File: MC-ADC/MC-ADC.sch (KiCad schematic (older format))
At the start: 11 parts, among them J1 86094327313755E1LF, U2 SZCM1213A-04SO

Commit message: ADC
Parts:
- removed C?: C_Small, symbol Device:C_Small
- removed R?: R_Small_US, symbol Device:R_Small_US
- removed U?: LM324DTBR2G, symbol MC-ADC:LM324DTBR2G
- added C?: C_Small, symbol Device:C_Small
- added R?: R_Small_US, symbol Device:R_Small_US
- added U?: LM339DR, symbol MC-ADC:LM339DR
- U?: symbol MC-ADC:LM324DTBR2G -> MC-ADC-rescue:LM324DTBR2G-MC-ADC
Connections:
- net labels added: -12V, ADCIN1, ADCIN2, ADCIN3, SAFE_STATE_FLAG
- net labels removed: ADCINA2, ADCINA4, ADCINB2
- wire segments 161 -> 232
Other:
- note added: "Edge Connector - Amphenol\nNeed to update\n"
- note added: "notes\n"
- note removed: "Edge Connector - Amphenol"
- moved on the sheet: C1, J1, R1, R2, R3, R4

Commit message: ADC Work
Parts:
- removed U2: SZCM1213A-04SO, symbol MC-ADC:SZCM1213A-04SO
- removed U?: LM339DR, symbol MC-ADC:LM339DR
- added R? (x6): 1.5K, symbol Device:R_Small_US
- added R? (x3): 5K, symbol Device:R_Small_US
- added R? (x3): 1.75K, symbol Device:R_Small_US
- added U? (x2): LM358, symbol MC-ADC:LM358
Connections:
- net labels added: -5V, 0V, 3V, 5V
- net labels removed: 1.5V
- wire segments 232 -> 229

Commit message: ADC Work
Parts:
- removed C1: DNP, symbol Device:C_Small
- removed C?: C_Small, symbol Device:C_Small
- removed R1: 100R, symbol Device:R_Small_US
- removed R2: 20R, symbol Device:R_Small_US
- removed R3, R4: 0R, symbol Device:R_Small_US
- removed R?: R_Small_US, symbol Device:R_Small_US
- removed R? (x6): 1.5K, symbol Device:R_Small_US
- removed R? (x3): 5K, symbol Device:R_Small_US
- removed R? (x3): 1.75K, symbol Device:R_Small_US
- removed U? (x2): LM358, symbol MC-ADC:LM358
- added C80, C84, C85: 43 nF, Capacitor_SMD:C_0805_2012Metric, symbol Device:C_Small
- added C81, C82, C83: 470 pF, Capacitor_SMD:C_1206_3216Metric, symbol Device:C_Small
- added R80, R84, R85: 2.2K, Resistor_SMD:R_1206_3216Metric, symbol Device:R_Small_US
- added R81, R82, R83: 330R, Resistor_SMD:R_0603_1608Metric, symbol Device:R_Small_US
- added U82: LT6238CGN#PBF, symbol MC-ADC:LT6238CGN#PBF
- U81: renamed from U?; footprint (none) -> Footprints_MC-ADC:LM324DTBR2G
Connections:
- net labels added: -0V4, 1.3V, 3V3, OUT_A, OUT_B, OUT_C
- net labels removed: -5V, 0V, 3V, 5V, ADCINA0, GND, GND2
- wire segments 229 -> 218
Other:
- note added: "Edge Connector - Amphenol\n"
- note added: "monitoring?\n"
- note removed: "3 BNC connectors on 2 cards\n"
- note removed: "BW calcs to meet requirements"
- note removed: "Edge Connector - Amphenol\nNeed to update\n"
- note removed: "Filter -> SAR ADC"
- note removed: "Need to deal with driving SAR ADCs"
- note removed: "notes\n"
- note removed: "post CDR\n"
- note removed: "to connector & then DSP\n"
- moved on the sheet: J1

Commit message: ADC Work + Start Layout
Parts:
- added R86: 10K, Resistor_SMD:R_1206_3216Metric, symbol Device:R_Small_US
- J1: footprint (none) -> Footprints_MC-ADC:86094327313755E1LF
- U82: footprint (none) -> Package_SO:SSOP-16_3.9x4.9mm_P0.635mm
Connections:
- net 1.3V: now also U82.12 (+IN_C); no longer U82.11 (-IN_C)
- net 3V3: now also R86.2
- net SAFE_STATE_FLAG: now also R86.1
- net at C82.1, C85.1, R82.1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: now also U82.11 (-IN_C); no longer U82.12 (+IN_C)
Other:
- note added: "monitoring not necessary?\n"
- note removed: "monitoring?\n"
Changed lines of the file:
@@
 F 0 "J1" H 10250 2667 50  0000 C CNN
 F 1 "86094327313755E1LF" H 10250 2576 50  0000 C CNN
-F 2 "" H 10200 1750 50  0001 C CNN
-F 3 "" H 10200 1750 50  0001 C CNN
+F 2 "Footprints_MC-ADC:86094327313755E1LF" H 10200 1750 50  0001 C CNN
+F 3 "https://www.mouser.com/ProductDetail/649-94327313755E1LF" H 10200 1750 50  0001 C CNN
 	1    10200 1750
 	1    0    0    -1
@@
 	10500 1950 10600 1950
 $Comp
-L power:GND1 #PWR?
+L power:GND1 #PWR0101
 U 1 1 620E7EB3
 P 10250 2800
-F 0 "#PWR?" H 10250 2550 50  0001 C CNN
+F 0 "#PWR0101" H 10250 2550 50  0001 C CNN
 F 1 "GND1" H 10255 2627 50  0000 C CNN
 F 2 "" H 10250 2800 50  0001 C CNN
@@
 Wire Notes Line
 	9050 650  11100 650
-Text GLabel 3300 1300 0    50   Input ~ 0
--12V
-Wire Wire Line
-	3300 1300 3400 1300
 Text GLabel 900  3850 0    50   Input ~ 0
 -12V
 Wire Wire Line
 	3650 1450 3650 2800
-Connection ~ 3400 1300
 Wire Wire Line
 	3400 1300 3400 2950
-Text GLabel 750  1050 2    50   Input ~ 0
+Text GLabel 1850 1550 2    50   Input ~ 0
 SAFE_STATE_FLAG
 Wire Wire Line
@@
 Connection ~ 10600 2550
 $Comp
-L power:GND1 #PWR?
+L power:GND1 #PWR0102
 U 1 1 6230238F
 P 5600 7350
-F 0 "#PWR?" H 5600 7100 50  0001 C CNN
+F 0 "#PWR0102" H 5600 7100 50  0001 C CNN
 F 1 "GND1" H 5605 7177 50  0000 C CNN
 F 2 "" H 5600 7350 50  0001 C CNN
@@
 $EndComp
 $Comp
-L power:GND1 #PWR?
+L power:GND1 #PWR0103
 U 1 1 62303055
 P 1050 4750
-F 0 "#PWR?" H 1050 4500 50  0001 C CNN
+F 0 "#PWR0103" H 1050 4500 50  0001 C CNN
 F 1 "GND1" H 1055 4577 50  0000 C CNN
 F 2 "" H 1050 4750 50  0001 C CNN
@@
 F 0 "U82" H 7750 3415 50  0000 C CNN
 F 1 "LT6238CGN#PBF" H 7750 3324 50  0000 C CNN
-F 2 "" H 7750 3450 50  0001 C CNN
-F 3 "" H 7750 3450 50  0001 C CNN
+F 2 "Package_SO:SSOP-16_3.9x4.9mm_P0.635mm" H 7750 3450 50  0001 C CNN
+F 3 "https://www.mouser.com/ProductDetail/Analog-Devices/LT6238CGNPBF?qs=hVkxg5c3xu%2F%2FmHiAJ8qs2Q%3D%3D" H 7750 3450 50  0001 C CNN
 	1    7750 3450
 	1    0    0    -1
@@
 Wire Wire Line
 	6900 4050 7000 4050
-Text GLabel 8600 4500 2    50   Input ~ 0
+Text GLabel 8600 4350 2    50   Input ~ 0
 1.3V
 Wire Wire Line
-	8600 4500 8300 4500
+	8600 4350 8300 4350
 Wire Wire Line
 	7000 4050 7000 4350
@@
 	6050 6000 8950 6000
 Wire Wire Line
-	8300 4350 8950 4350
+	8300 4500 8950 4500
 $Comp
 L Device:R_Small_US R82
@@
 Connection ~ 8950 4750
 Wire Wire Line
-	8950 4750 8950 4350
+	8950 4750 8950 4500
 Wire Wire Line
 	8750 4750 8950 4750
@@
 	8450 3900 8650 3900
 $Comp
-L power:GND1 #PWR?
+L power:GND1 #PWR0104
 U 1 1 62A0E39B
 P 8650 3900
-F 0 "#PWR?" H 8650 3650 50  0001 C CNN
+F 0 "#PWR0104" H 8650 3650 50  0001 C CNN
 F 1 "GND1" H 8655 3727 50  0000 C CNN
 F 2 "" H 8650 3900 50  0001 C CNN
@@
 OUT_C
 Wire Notes Line
-	550  1300 1600 1300
+	1550 1700 2600 1700
 Wire Notes Line
-	1600 1300 1600 850
+	2600 800  1550 800
+Text Notes 1550 750  0    50   ~ 0
+monitoring not necessary?\n
 Wire Notes Line
-	1600 850  550  850
+	2600 800  2600 1700
 Wire Notes Line
-	550  850  550  1300
-Text Notes 750  750  0    50   ~ 0
-monitoring?\n
+	1550 800  1550 1700
+$Comp
+L Device:R_Small_US R?
+U 1 1 622E9955
+P 1800 1200
+AR Path="/61F0AAD9/622E9955" Ref="R?"  Part="1"
+AR Path="/61F25080/622E9955" Ref="R?"  Part="1"
+AR Path="/622E9955" Ref="R86"  Part="1"
+AR Path="/620D84A4/622E9955" Ref="R?"  Part="1"
+AR Path="/620D8862/622E9955" Ref="R?"  Part="1"
+AR Path="/620D8F0D/622E9955" Ref="R?"  Part="1"
+F 0 "R86" H 1650 1150 50  0000 C CNN
+F 1 "10K" H 1650 1250 50  0000 C CNN
+F 2 "Resistor_SMD:R_1206_3216Metric" H 1800 1200 50  0001 C CNN
+F 3 "~" H 1800 1200 50  0001 C CNN
+	1    1800 1200
+	1    0    0    1
+$EndComp
+Wire Wire Line
+	1800 1550 1850 1550
+Wire Wire Line
+	1800 1550 1800 1300
+Wire Wire Line
+	1800 1100 1800 900
+Wire Wire Line
+	1800 900  1850 900
+Text GLabel 1850 900  2    50   Input ~ 0
+3V3
 $EndSCHEMATC

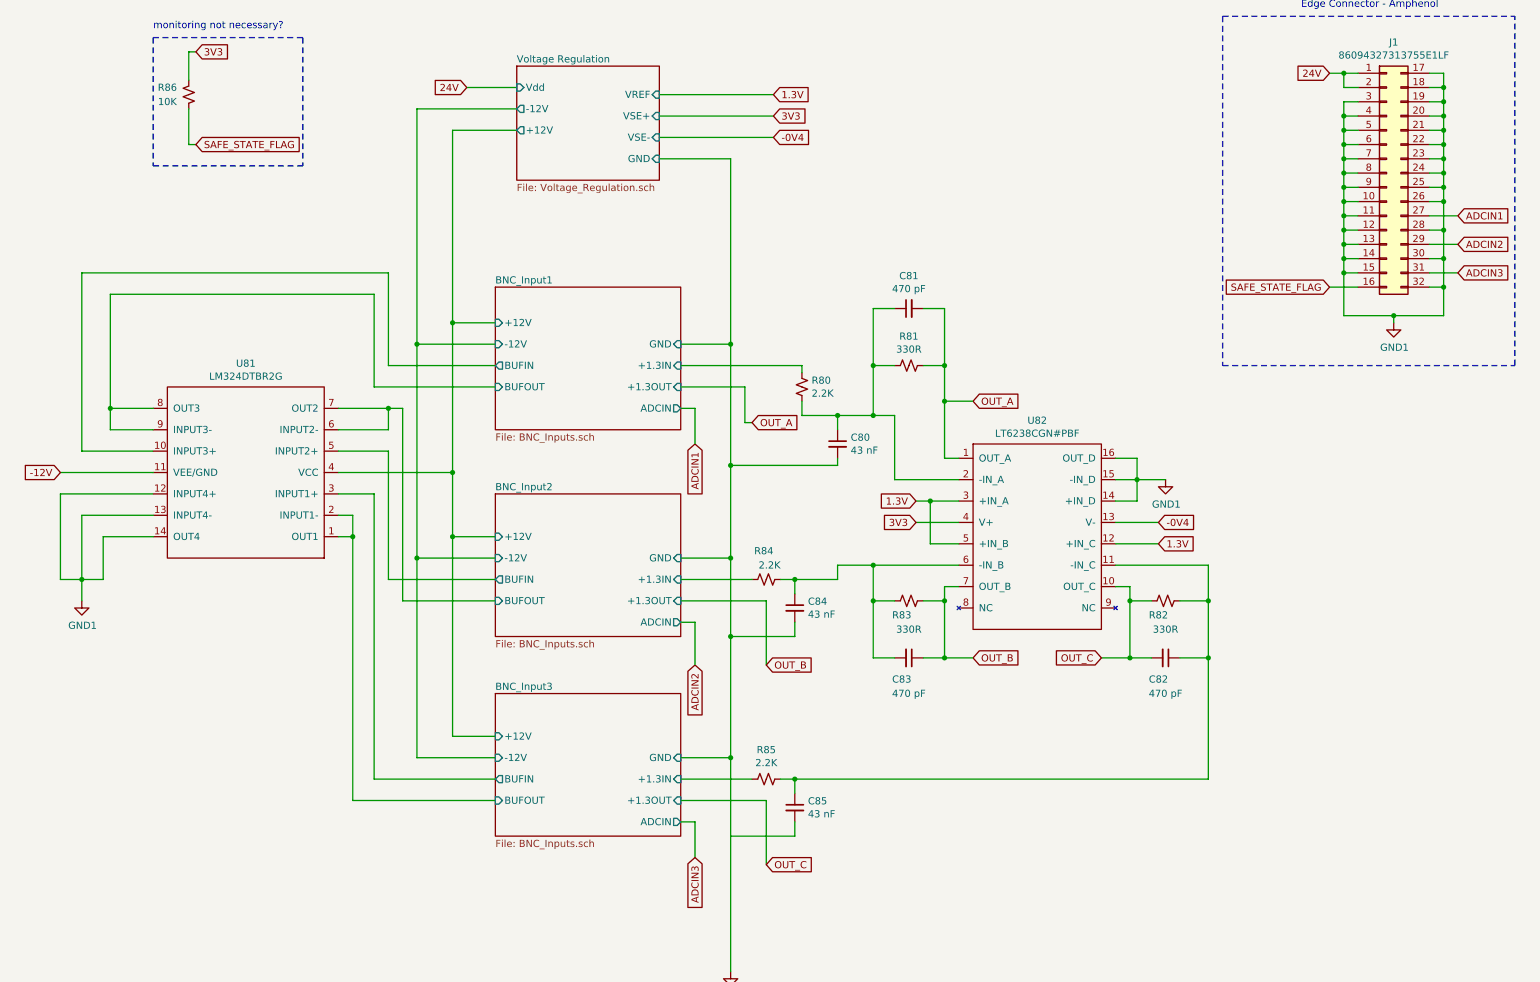
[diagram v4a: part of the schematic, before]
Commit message: ADC Work + Layout
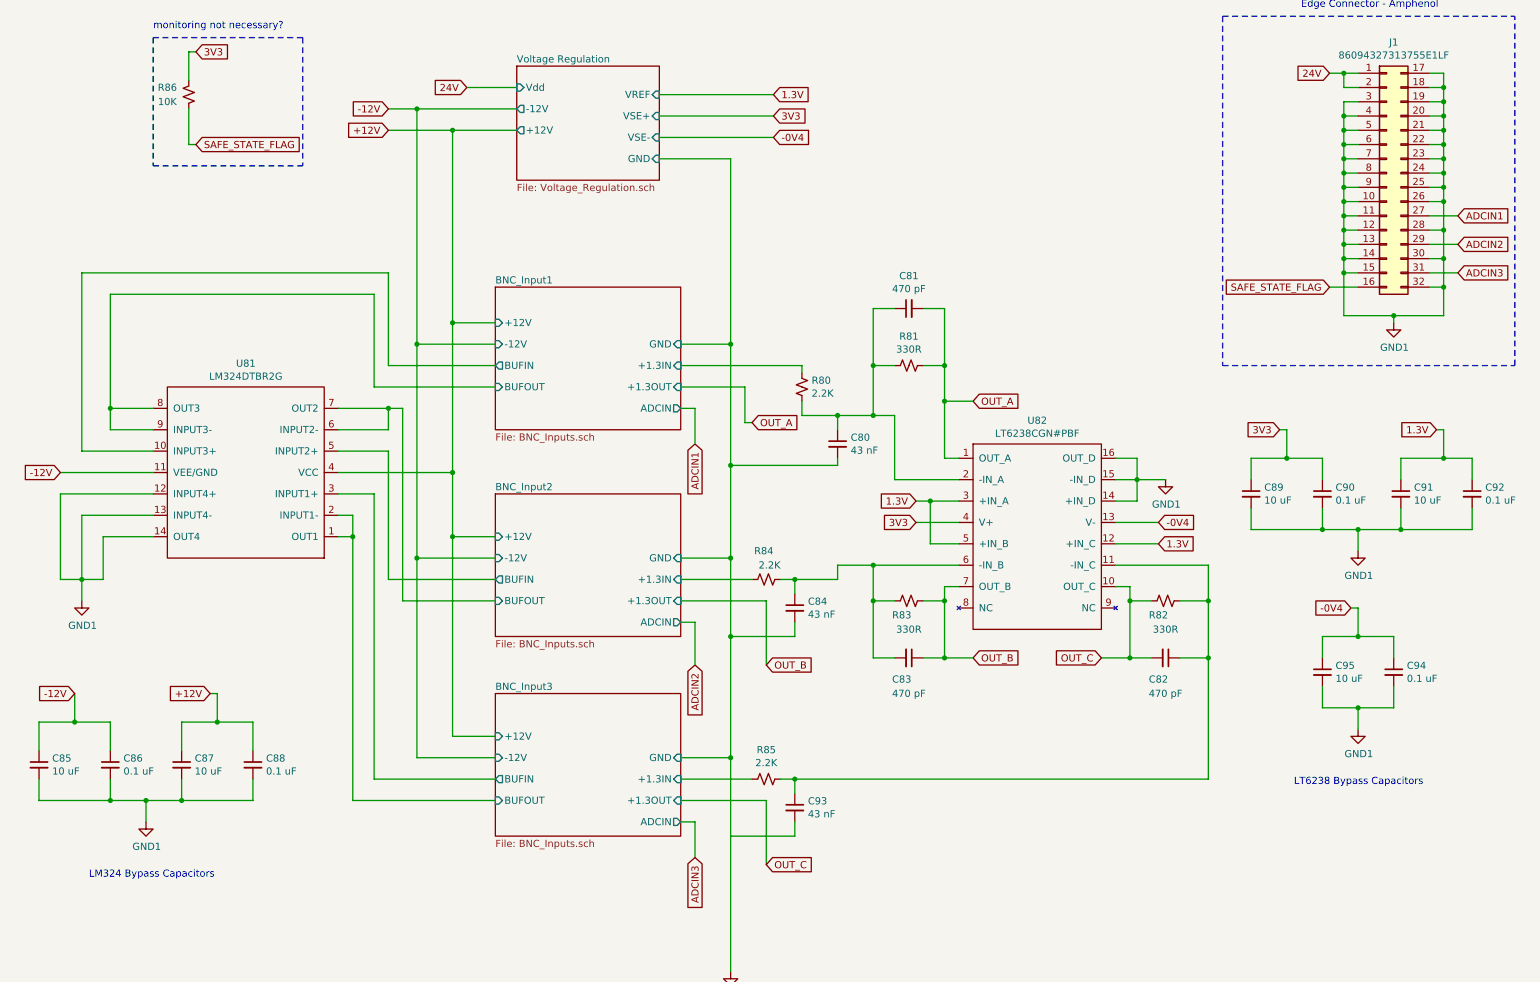
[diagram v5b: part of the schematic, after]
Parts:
- added C85, C87, C89, C91, C95: 10 uF, Capacitor_SMD:C_1210_3225Metric, symbol Device:C_Small
- added C86, C88, C90, C92, C94: 0.1 uF, Capacitor_SMD:C_1210_3225Metric, symbol Device:C_Small
- renumbered C85 to C93
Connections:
- net -0V4: now also C94.1, C95.1
- net -12V: now also C85.1, C86.1
- net 1.3V: now also C91.1, C92.1
- net 3V3: now also C89.1, C90.1
- net GND1: now also C85.2, C86.2, C87.2, C88.2, C89.2, C90.2, C91.2, C92.2, C94.2, C95.2
- net BNC_Input1/+12V renamed +12V
- net +12V: now also C87.1, C88.1
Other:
- note added: "LM324 Bypass Capacitors"
- note added: "LT6238 Bypass Capacitors"

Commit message: ADC work for Alpha
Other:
- note added: "monitoring not necessary."
- note removed: "monitoring not necessary?\n"
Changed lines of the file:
@@
 	2600 800  1550 800
 Text Notes 1550 750  0    50   ~ 0
-monitoring not necessary?\n
+monitoring not necessary.
 Wire Notes Line
 	2600 800  2600 1700

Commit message: ADC LAYOUT
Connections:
- net GND1: now also C93.2
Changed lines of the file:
@@
 Connection ~ 5600 5850
 Wire Wire Line
-	5600 5850 5600 7350
+	5600 5850 5600 6400
 Wire Wire Line
 	5250 3400 5350 3400
@@
 Wire Wire Line
 	10000 5000 10250 5000
+Connection ~ 5600 6400
+Wire Wire Line
+	5600 6400 5600 7350
 $EndSCHEMATC

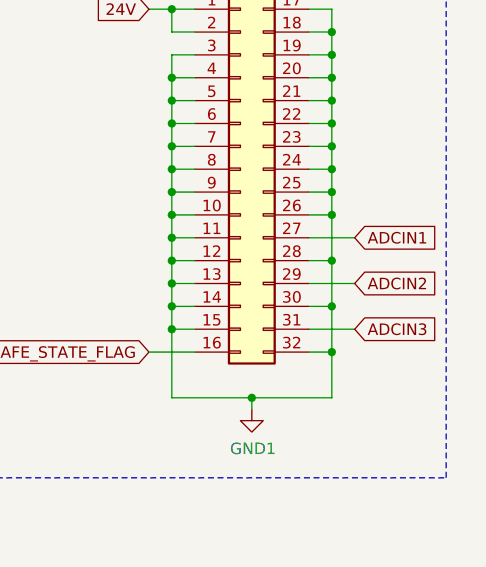
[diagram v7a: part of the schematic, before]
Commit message: Prelim ADC layout complete
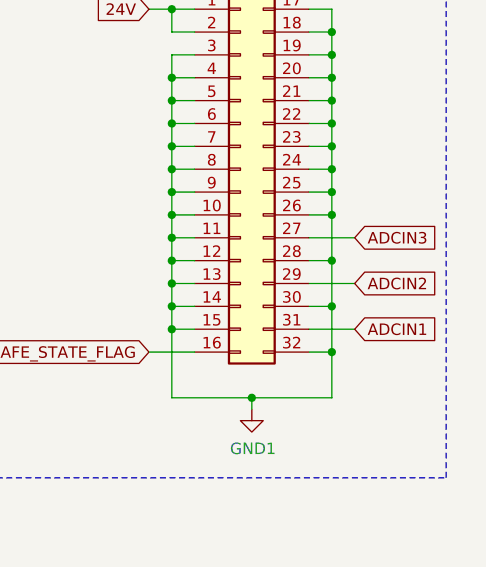
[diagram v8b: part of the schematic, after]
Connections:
- net ADCIN1: now also J1.31 (Pin_31); no longer J1.27 (Pin_27)
- net ADCIN3: now also J1.27 (Pin_27); no longer J1.31 (Pin_31)
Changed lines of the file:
@@
 	4100 1150 3750 1150
 Text GLabel 10700 2450 2    50   Input ~ 0
-ADCIN3
+ADCIN1
 Text GLabel 10700 2250 2    50   Input ~ 0
 ADCIN2
@@
 	5350 4900 5350 5200
 Text GLabel 10700 2050 2    50   Input ~ 0
-ADCIN1
+ADCIN3
 Text GLabel 5350 5200 3    50   Input ~ 0
 ADCIN2
